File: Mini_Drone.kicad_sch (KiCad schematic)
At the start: 67 parts, among them J1 Conn_01x02, J3 Conn_01x02, J4 Conn_01x06, J7 Conn_01x11, J8 Conn_01x11, Q1 AO3400A, Q2 AO3400A, Q3 AO3400A, Q4 AO3400A, SW2 Tactile Switch 3x4x2, SW3 Tactile Switch 3x4x2, U1 ESP32-S3-WROOM-1, U2 MPU_6050_Module, U3 SPX3819M5-L-3-3

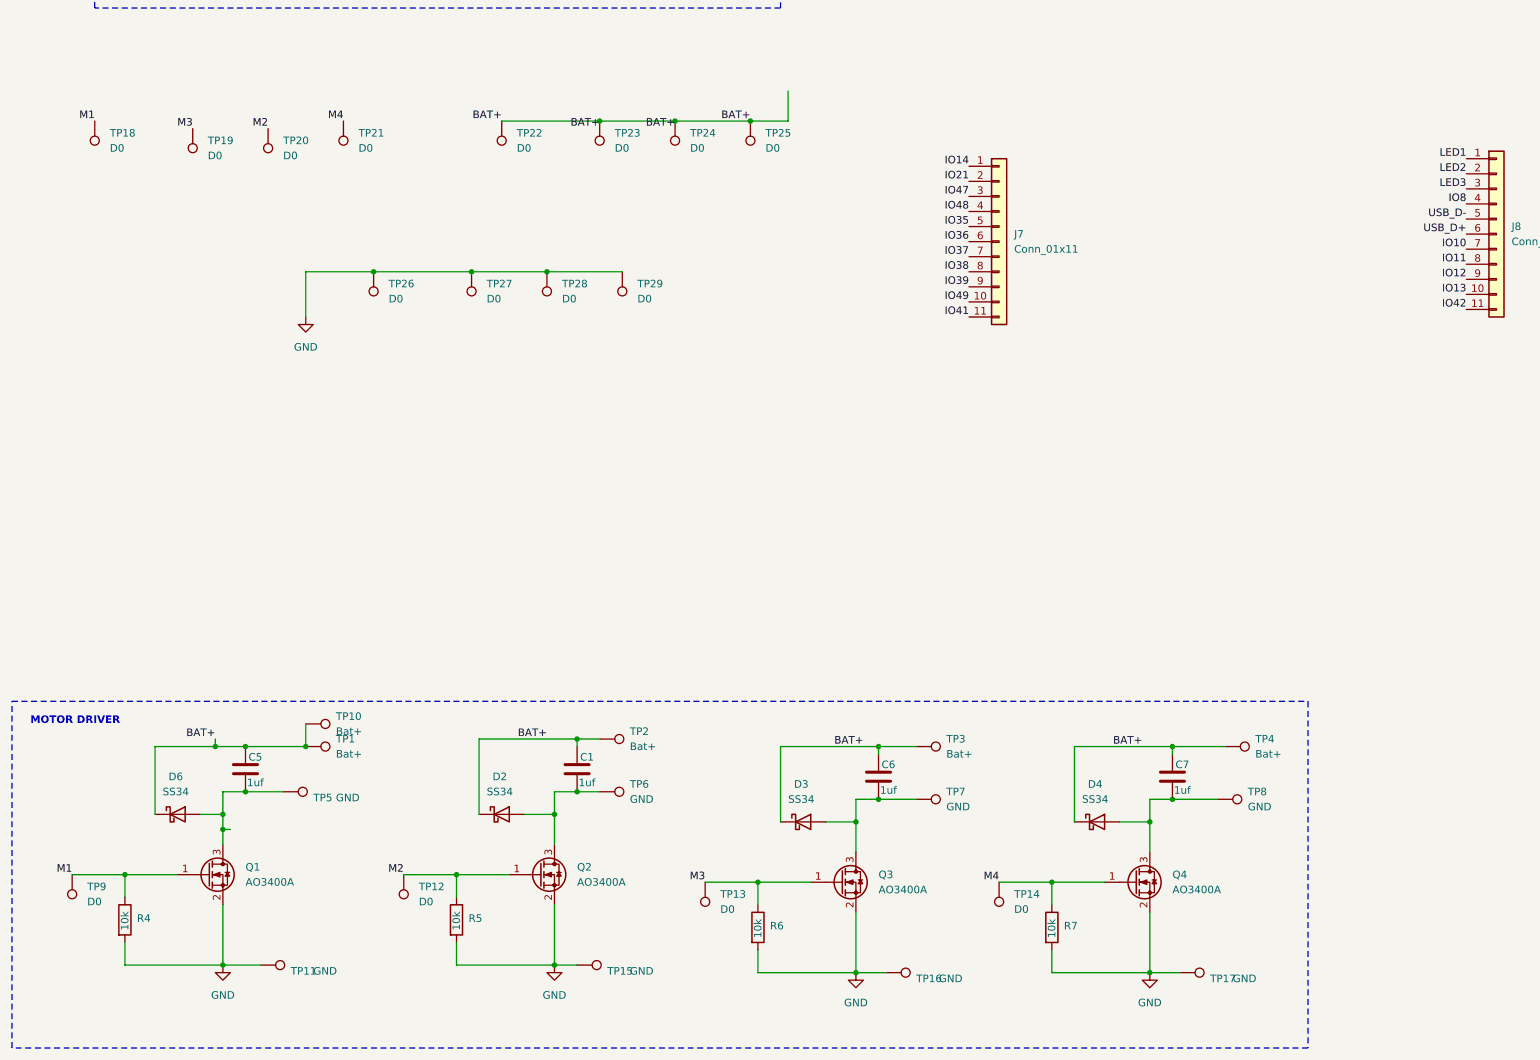
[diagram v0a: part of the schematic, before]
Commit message: main board completed need to tidy up the routing , motor driver yet to be completed
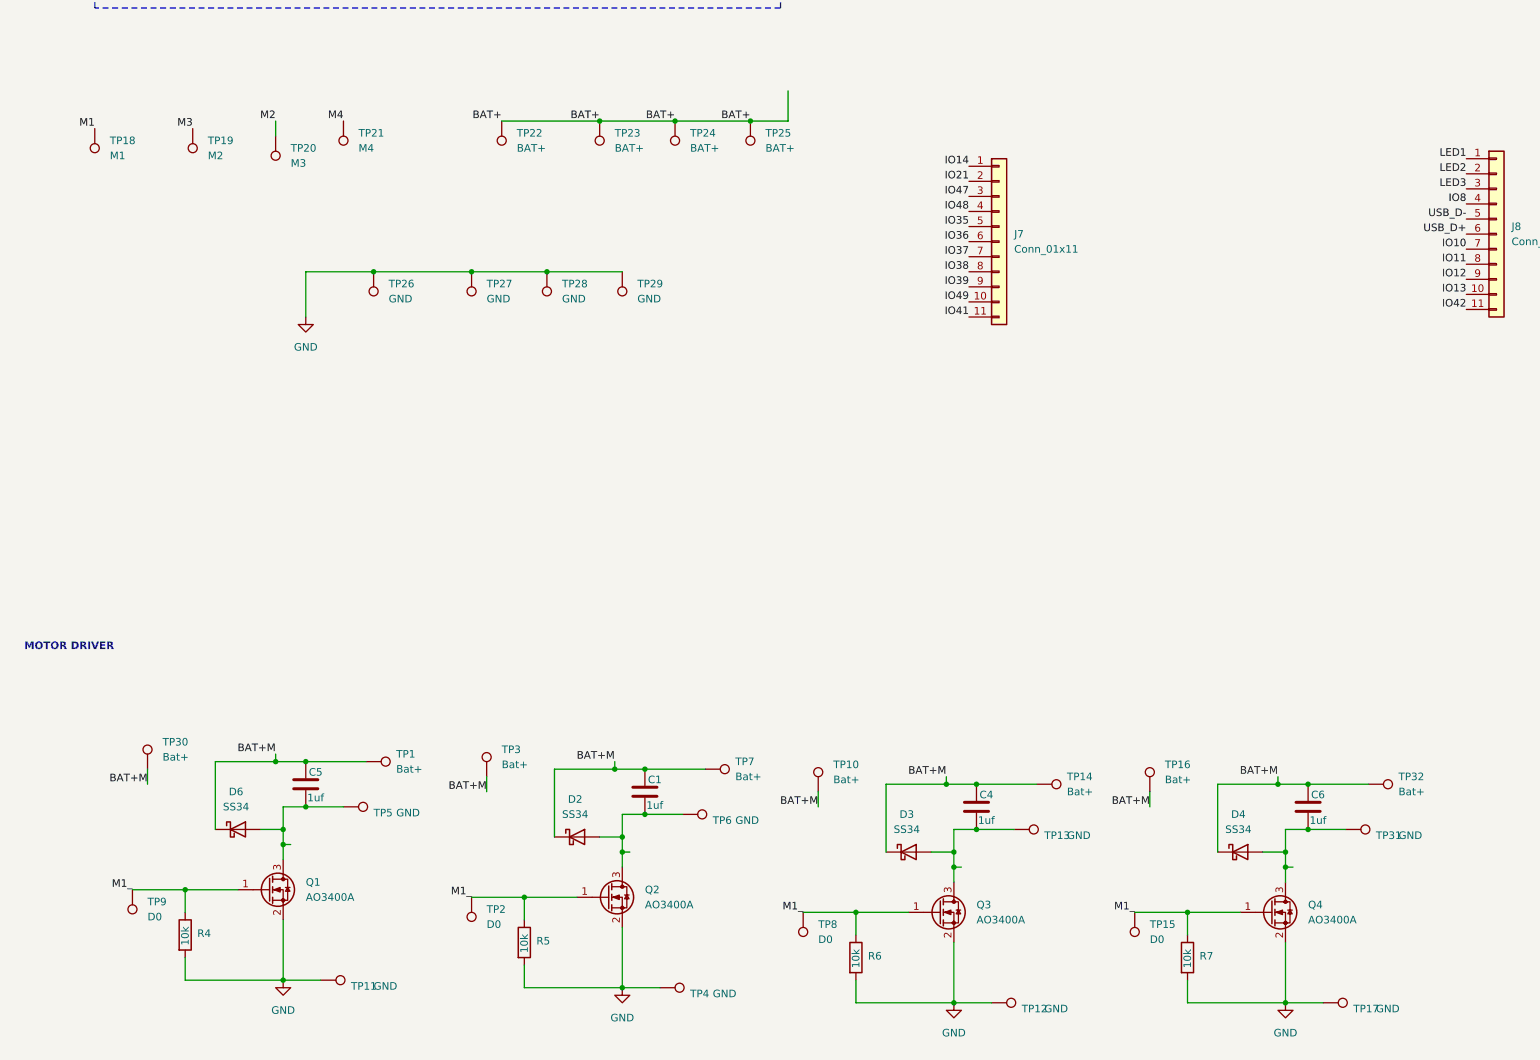
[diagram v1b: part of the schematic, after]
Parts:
- removed C7: 1uf, Capacitor_SMD:C_0603_1608Metric, symbol Device:C
- added C4: 1uf, Capacitor_SMD:C_0603_1608Metric, symbol Device:C
- added TP30, TP32: Bat+, TestPoint:TestPoint_Pad_D1.0mm, symbol Connector:TestPoint
- added TP31: GND, TestPoint:TestPoint_Pad_D1.0mm, symbol Connector:TestPoint
- TP12, TP13, TP26, TP27, TP28, TP29: value D0 -> GND
- TP14: value D0 -> Bat+
- TP15, TP8: value GND -> D0
- TP16, TP7: value GND -> Bat+
- TP18: value D0 -> M1
- TP19: value D0 -> M2
- TP2: value Bat+ -> D0
- TP20: value D0 -> M3
- TP21: value D0 -> M4
- TP22, TP23, TP24, TP25: value D0 -> BAT+
- TP4: value Bat+ -> GND
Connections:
- net BAT+: no longer C1.1, C5.1, C6.1, D2.1 (K), D3.1 (K), D4.1 (K), D6.1 (K), TP1.1, TP10.1, TP2.1, TP3.1, TP4.1
- net GND: now also TP12.1, TP4.1; no longer TP15.1, TP16.1
- net M1: no longer Q1.1 (G), R4.1, TP9.1
- net M2: no longer Q2.1 (G), R5.1, TP12.1
- net M3: no longer Q3.1 (G), R6.1, TP13.1
- net M4: no longer Q4.1 (G), R7.1, TP14.1
- net at D3.2 (A), Q3.3 (D): now also TP13.1, C4.2; no longer C6.2, TP7.1
- net at D4.2 (A), Q4.3 (D): now also C6.2, TP31.1; no longer TP8.1
- new net BAT+M: C1.1, C4.1, C5.1, C6.1, D2.1 (K), D3.1 (K), D4.1 (K), D6.1 (K), TP1.1, TP10.1, TP14.1, TP16.1, TP3.1, TP30.1, TP32.1, TP7.1
- new net M1_: Q1.1 (G), Q2.1 (G), Q3.1 (G), Q4.1 (G), R4.1, R5.1, R6.1, R7.1, TP15.1, TP2.1, TP8.1, TP9.1
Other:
- moved on the sheet: C5, D6, Q1, R4, TP1, TP11, TP18, TP20, TP5, TP9

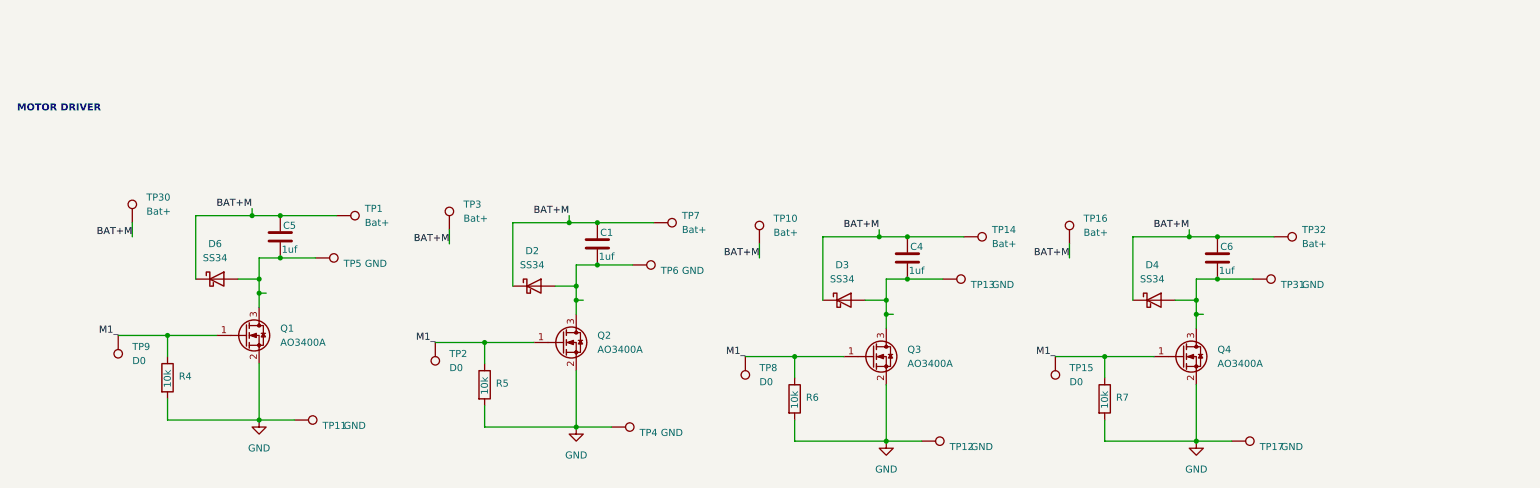
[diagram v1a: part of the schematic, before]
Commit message: motor driver circuit need to do the outline
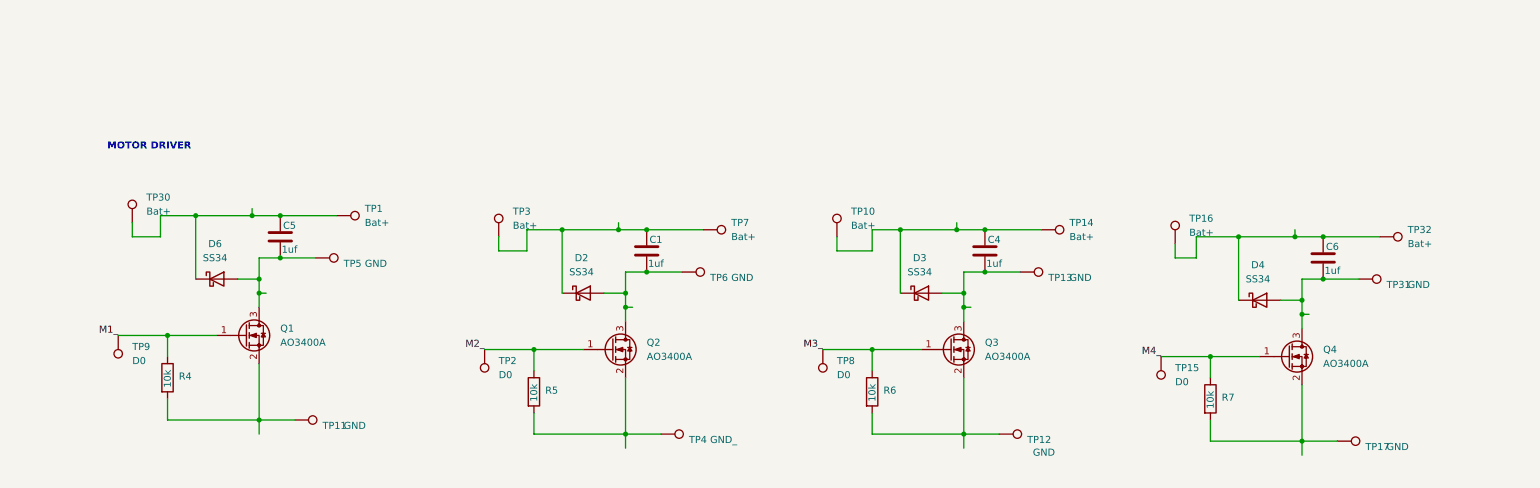
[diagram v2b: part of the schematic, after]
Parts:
- TP4: value GND -> GND_
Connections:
- net GND: no longer Q1.2 (S), Q2.2 (S), Q3.2 (S), Q4.2 (S), R4.2, R5.2, R6.2, R7.2, TP11.1, TP12.1, TP17.1, TP4.1
- net M1_: no longer Q2.1 (G), Q3.1 (G), Q4.1 (G), R5.1, R6.1, R7.1, TP15.1, TP2.1, TP8.1
- removed net BAT+M: C1.1, C4.1, C5.1, C6.1, D2.1 (K), D3.1 (K), D4.1 (K), D6.1 (K), TP1.1, TP10.1, TP14.1, TP16.1, TP3.1, TP30.1, TP32.1, TP7.1
- new net: C6.1, D4.1 (K), TP16.1, TP32.1
- new net: Q1.2 (S), R4.2, TP11.1
- new net: Q3.2 (S), R6.2, TP12.1
- new net: Q4.2 (S), R7.2, TP17.1
- new net: Q2.2 (S), R5.2, TP4.1
- new net: C1.1, D2.1 (K), TP3.1, TP7.1
- new net: C5.1, D6.1 (K), TP1.1, TP30.1
- new net: C4.1, D3.1 (K), TP10.1, TP14.1
- new net M2_: Q2.1 (G), R5.1, TP2.1
- new net M3_: Q3.1 (G), R6.1, TP8.1
- new net M4_: Q4.1 (G), R7.1, TP15.1

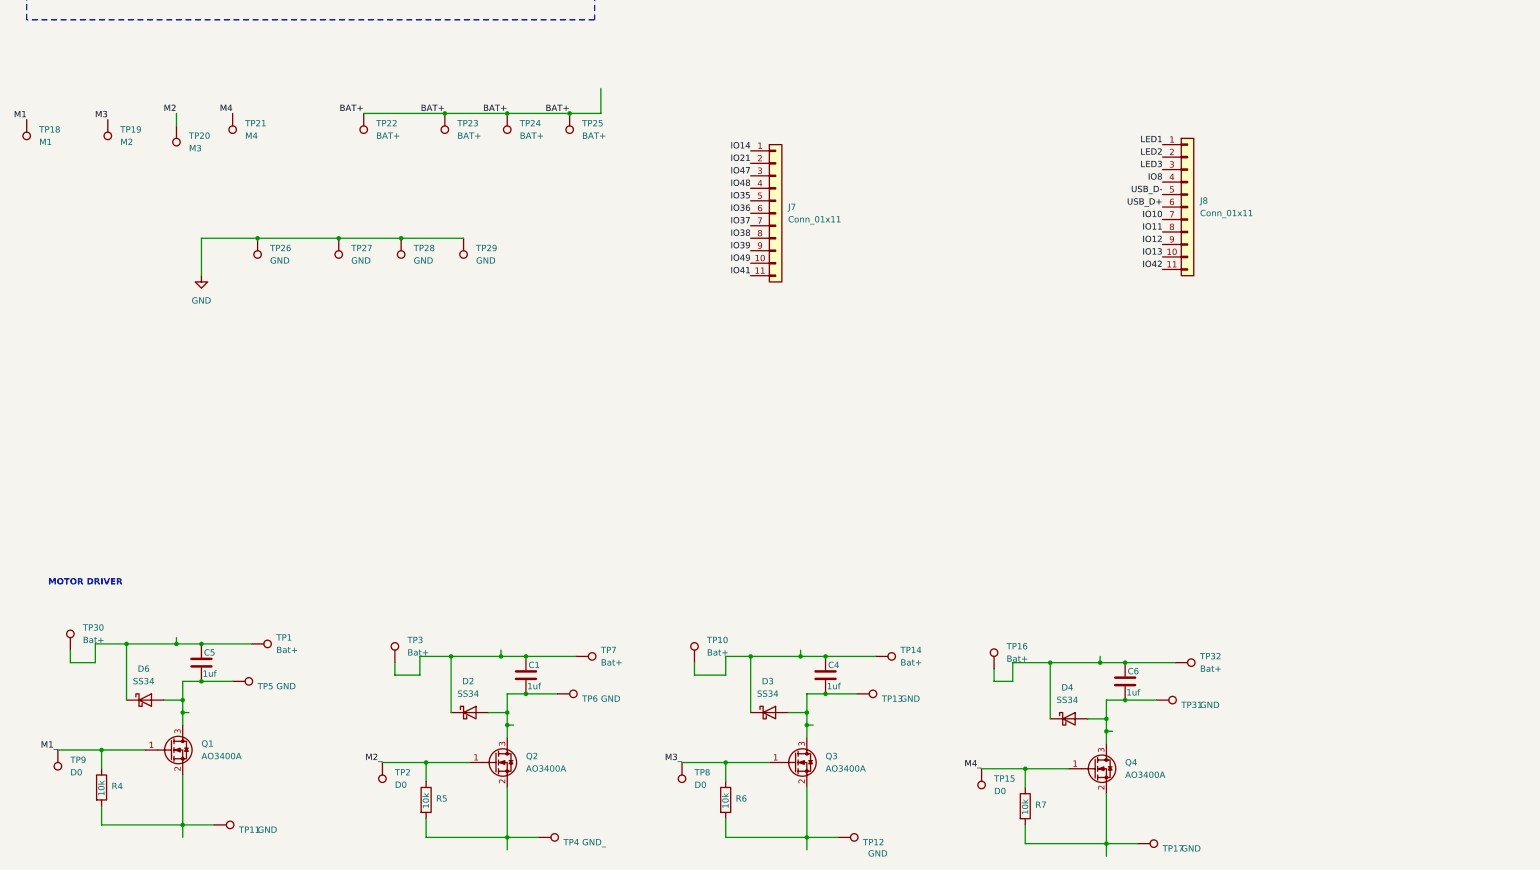
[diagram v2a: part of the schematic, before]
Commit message: need to make it perfect change the switch and led outline needs to be corrected
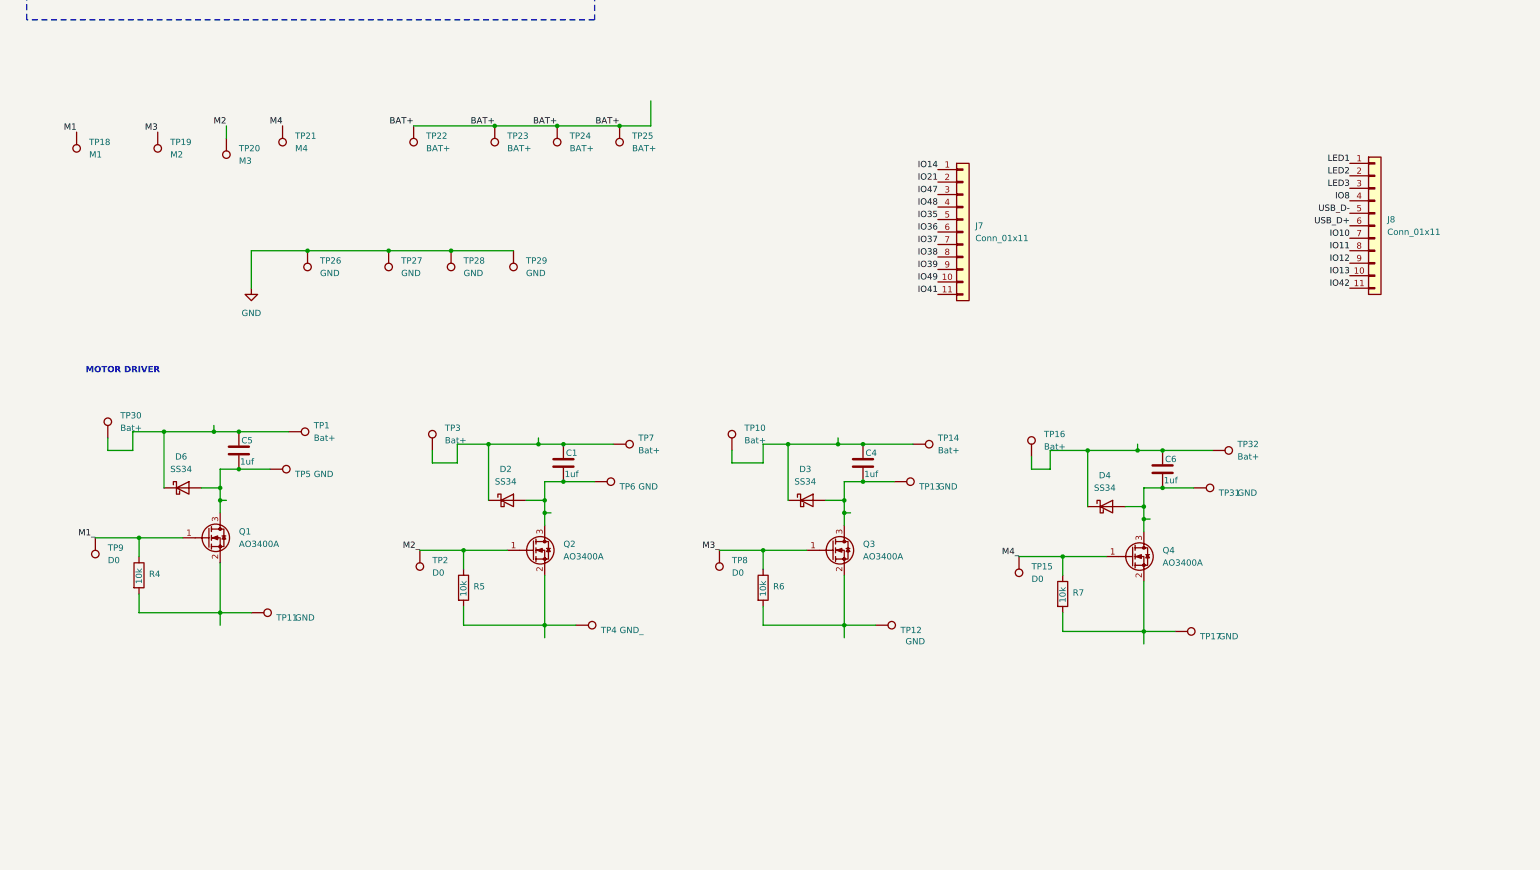
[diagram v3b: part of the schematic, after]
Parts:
- C1, C4, C5, C6, C8: LCSC Part # (none) -> C15849; LCSC Part# C15849 -> (none)
- C2: LCSC Part # (none) -> C59461; LCSC Part# C59461 -> (none)
- C3: LCSC Part # (none) -> C1620; LCSC Part# C1620 -> (none)
- C9: LCSC Part # (none) -> C14663; LCSC Part# C14663 -> (none)
- D1: LCSC Part # (none) -> C2994781
- D2, D3, D4, D6: LCSC Part # (none) -> C8678; LCSC Part# C8678 -> (none)
- D5: LCSC Part # (none) -> C19171390
- D7: LCSC Part # (none) -> C19171394
- J1, J4, J7, J8, TP1, TP10, TP11, TP12, TP13, TP14, TP15, TP16, TP17, TP18, TP19, TP2, TP20, TP21, TP22, TP23, TP24, TP25, TP26, TP27, TP28, TP29, TP3, TP30, TP31, TP32, TP4, TP5, TP6, TP7, TP8, TP9, U1, U2: now left out of the parts list
- J3: LCSC Part # (none) -> C160262; now left out of the parts list
- U3: LCSC Part # (none) -> C9055
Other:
- moved on the sheet: C1, C4, C5, C6, D2, D3, D4, D6, J7, J8, Q1, Q2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

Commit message: Hari's update
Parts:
- removed SW2, SW3: Tactile Switch 3x4x2, Button_Switch_SMD:SW_Push_SPST_NO_Alps_SKRK, symbol Switch:SW_Push
- added S1, S2: TL1105F160Q, Mini_Drone_prj:SW_TL1105F160Q, symbol TL1105F160Q:TL1105F160Q
- added S3: 100SP1T1B4M2QE, Mini_Drone_prj:SW_100SP1T1B4M2QE, symbol 100SP1T1B4M2QE:100SP1T1B4M2QE
- D1: LCSC Part # C2994781 -> C22371297
- D5: LCSC Part # C19171390 -> C965799
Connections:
- net BAT+: now also S3.1, S3.2
- net EN: now also S2.1, S2.2
- net GND: now also S1.3, S1.4, S2.3, S2.4
- net IO0: now also S1.1, S1.2
- net at R6.2, TP12.1: no longer Q3.2 (S)
- net at R7.2, TP17.1: no longer Q4.2 (S)
- net at R5.2, TP4.1: no longer Q2.2 (S)
- no-connect marks 4 -> 5

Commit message: Almost finished need to check it before the ordering need check all the violaition
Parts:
- removed S1, S2: TL1105F160Q, Mini_Drone_prj:SW_TL1105F160Q, symbol TL1105F160Q:TL1105F160Q
- removed S3: 100SP1T1B4M2QE, Mini_Drone_prj:SW_100SP1T1B4M2QE, symbol 100SP1T1B4M2QE:100SP1T1B4M2QE
- added S1, S3: TL1105F160Q, Mini_Drone_prj:SW_TL1105F160Q, symbol Mini_Drone_prj:TL1105F160Q
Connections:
- net EN: now also S3.1, S3.2
- net GND: now also S1.3, S1.4, S3.3, S3.4
- net IO0: now also S1.1, S1.2
- net at R6.2, TP12.1: now also Q3.2 (S)
- net at Q4.2 (S): now also R7.2, TP17.1
- net at R5.2, TP4.1: now also Q2.2 (S)
- no-connect marks 5 -> 4
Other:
- moved on the sheet: C1, C4, C5, C6, D2, D3, D4, D6, J7, Q1, Q2, Q3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
